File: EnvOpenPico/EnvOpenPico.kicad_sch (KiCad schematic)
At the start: 58 parts, among them J2 TSA343G00-250J2, J3 2.54mm header 01x20, J4 2.54mm header 01x20, J5 Conn_01x03_Male, Q1 SI2301B, U1 SOT-23-5 5.5V 3.3V 500mA, U3 RP2040, Y1 3225_4P

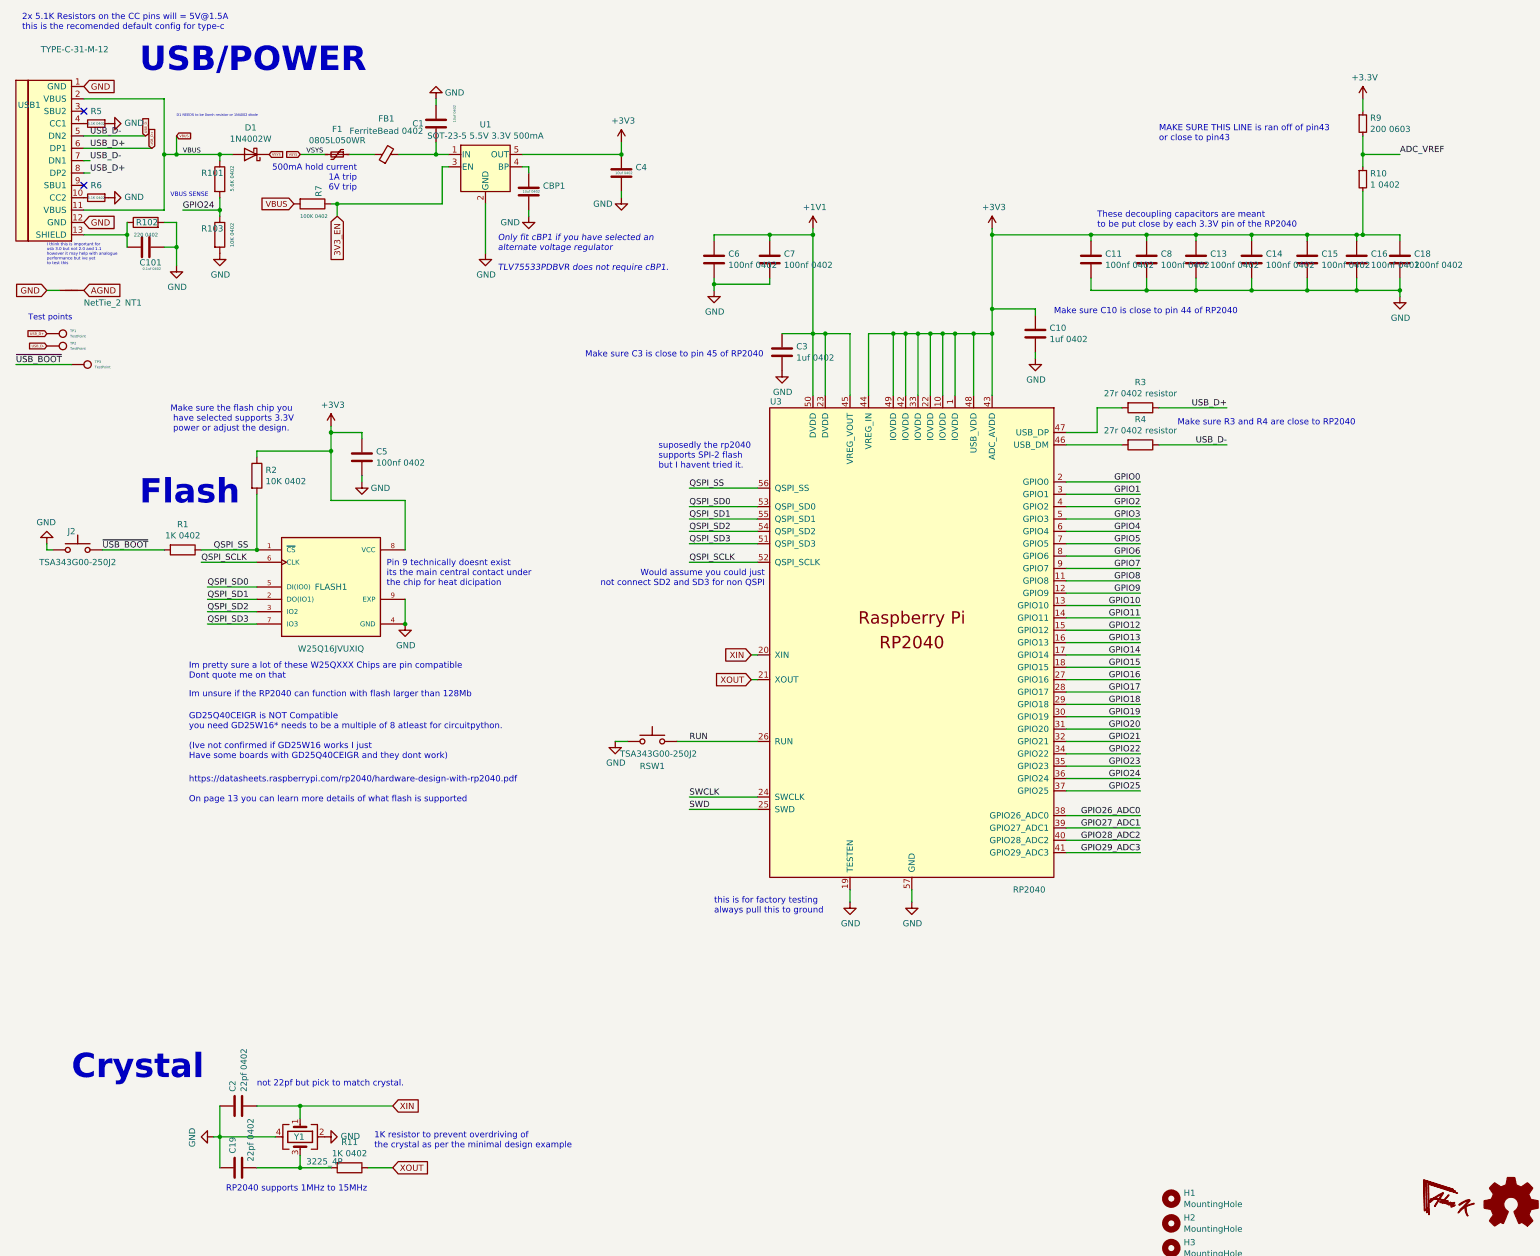
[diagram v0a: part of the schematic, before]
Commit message: replaced flash symbol with built in one, some clearance fixes
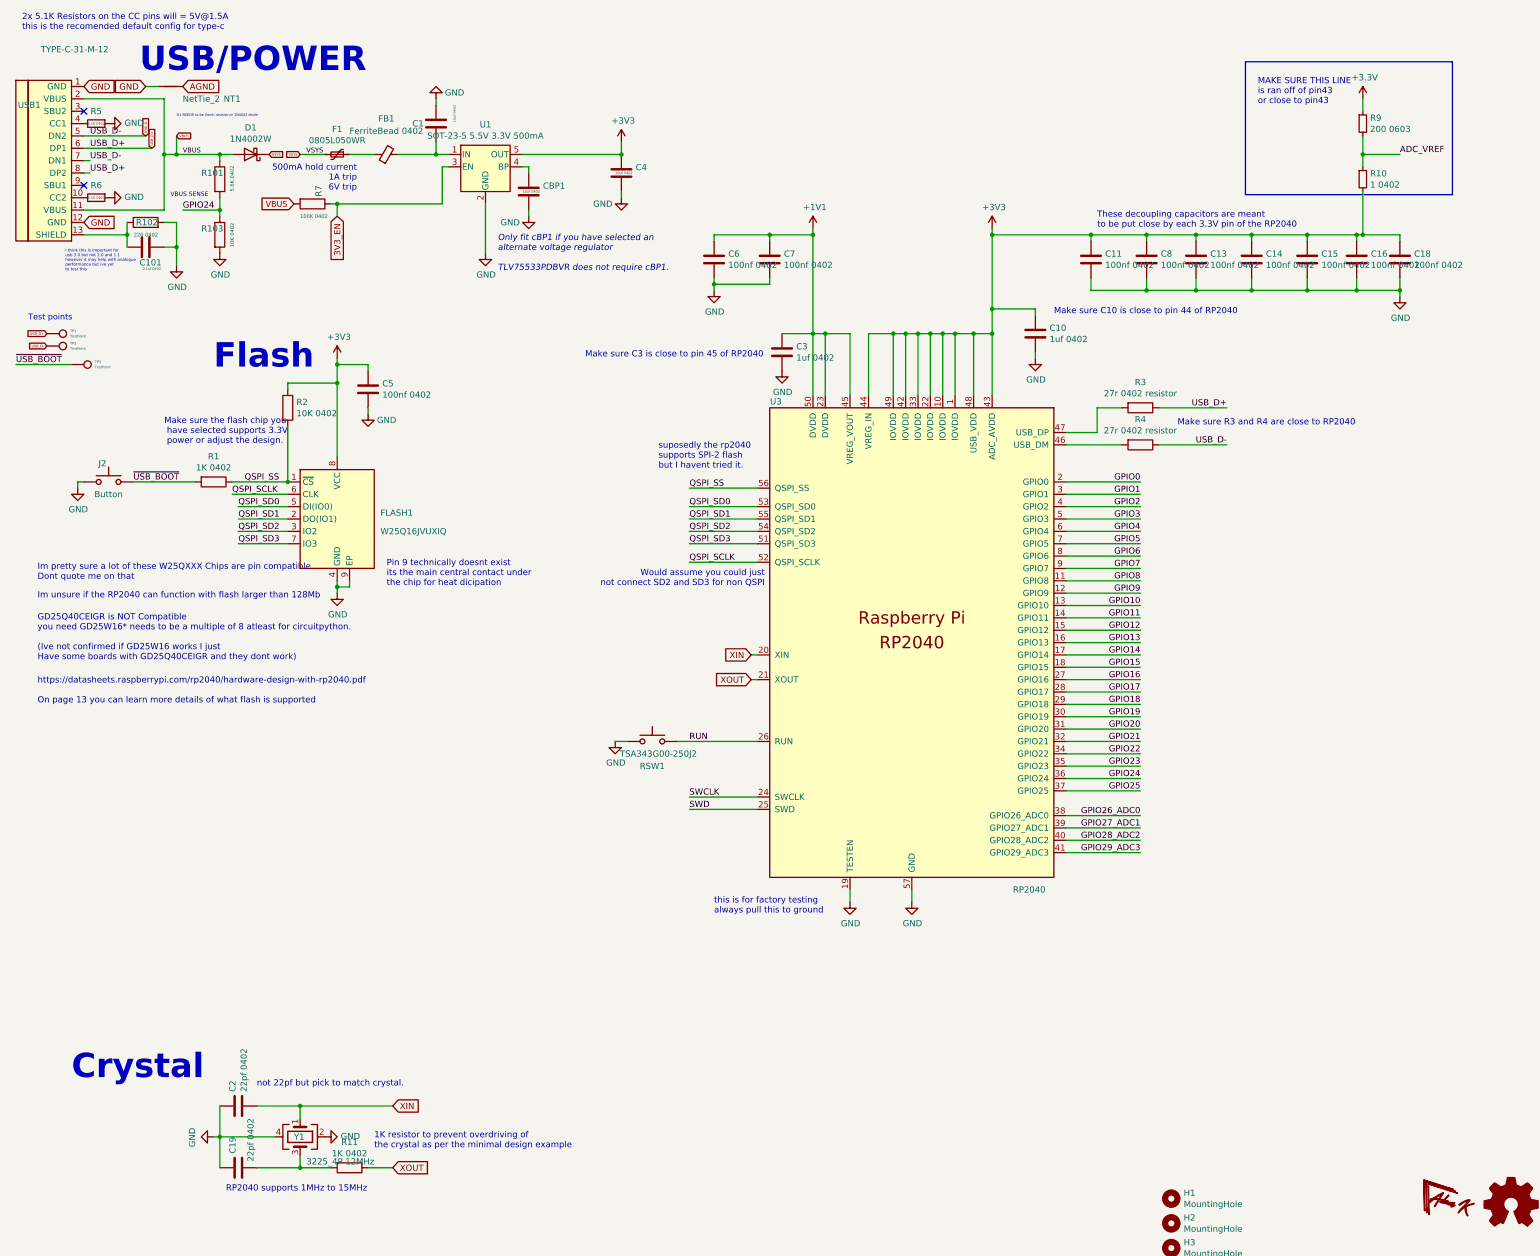
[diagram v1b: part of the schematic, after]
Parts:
- removed FLASH1: W25Q16JVUXIQ, Package_SON:SON-8-1EP_3x2mm_P0.5mm_EP1.4x1.6mm, symbol W25Q256JVEIQ_TR:W25Q256JVEIQ_TR
- added FLASH1: W25Q16JVUXIQ, Package_SON:SON-8-1EP_3x2mm_P0.5mm_EP1.4x1.6mm, symbol Memory_Flash:W25Q32JVZP
- J2: value TSA343G00-250J2 -> Button
- Y1: value 3225_4P -> 3225_4P 12MHz
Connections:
- net +3V3: now also FLASH1.8 (VCC)
- net GND: now also FLASH1.4 (GND), FLASH1.9 (EP)
- net QSPI_SCLK: now also FLASH1.6 (CLK)
- net QSPI_SD0: now also FLASH1.5 (DI(IO0))
- net QSPI_SD1: now also FLASH1.2 (DO(IO1))
- net QSPI_SD2: now also FLASH1.3 (IO2)
- net QSPI_SD3: now also FLASH1.7 (IO3)
- net QSPI_SS: now also FLASH1.1 (~{CS})
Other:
- title: Raspberry Pi Pico Clone -> EnvOpenPico
- moved on the sheet: NT1

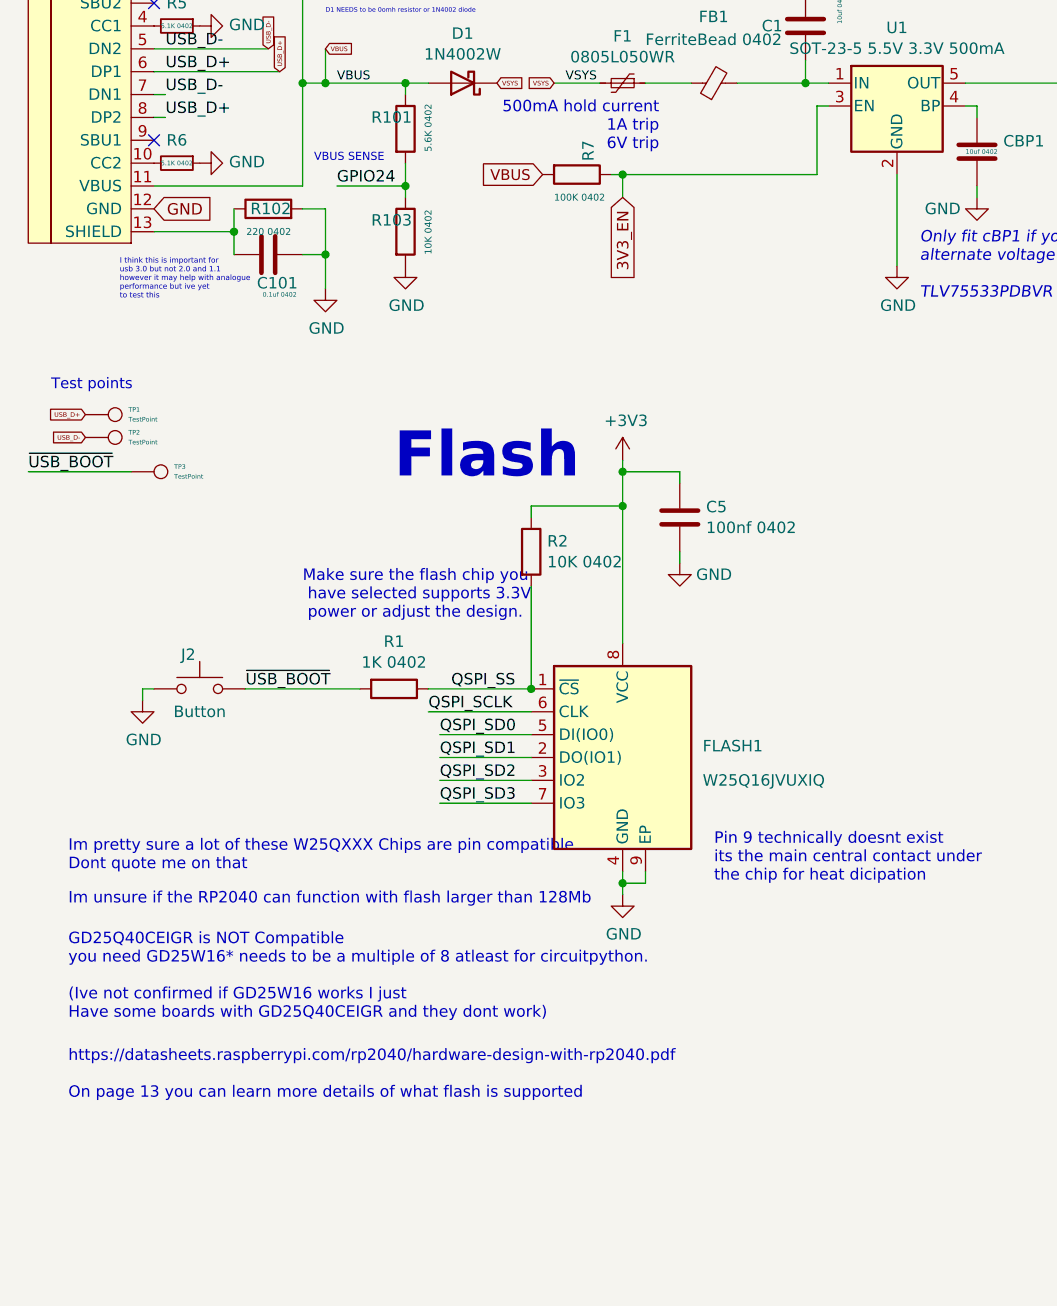
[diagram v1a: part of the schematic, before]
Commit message: fixed major potential oversight on 3V3_EN being tied to VBUS rather than VSYS.
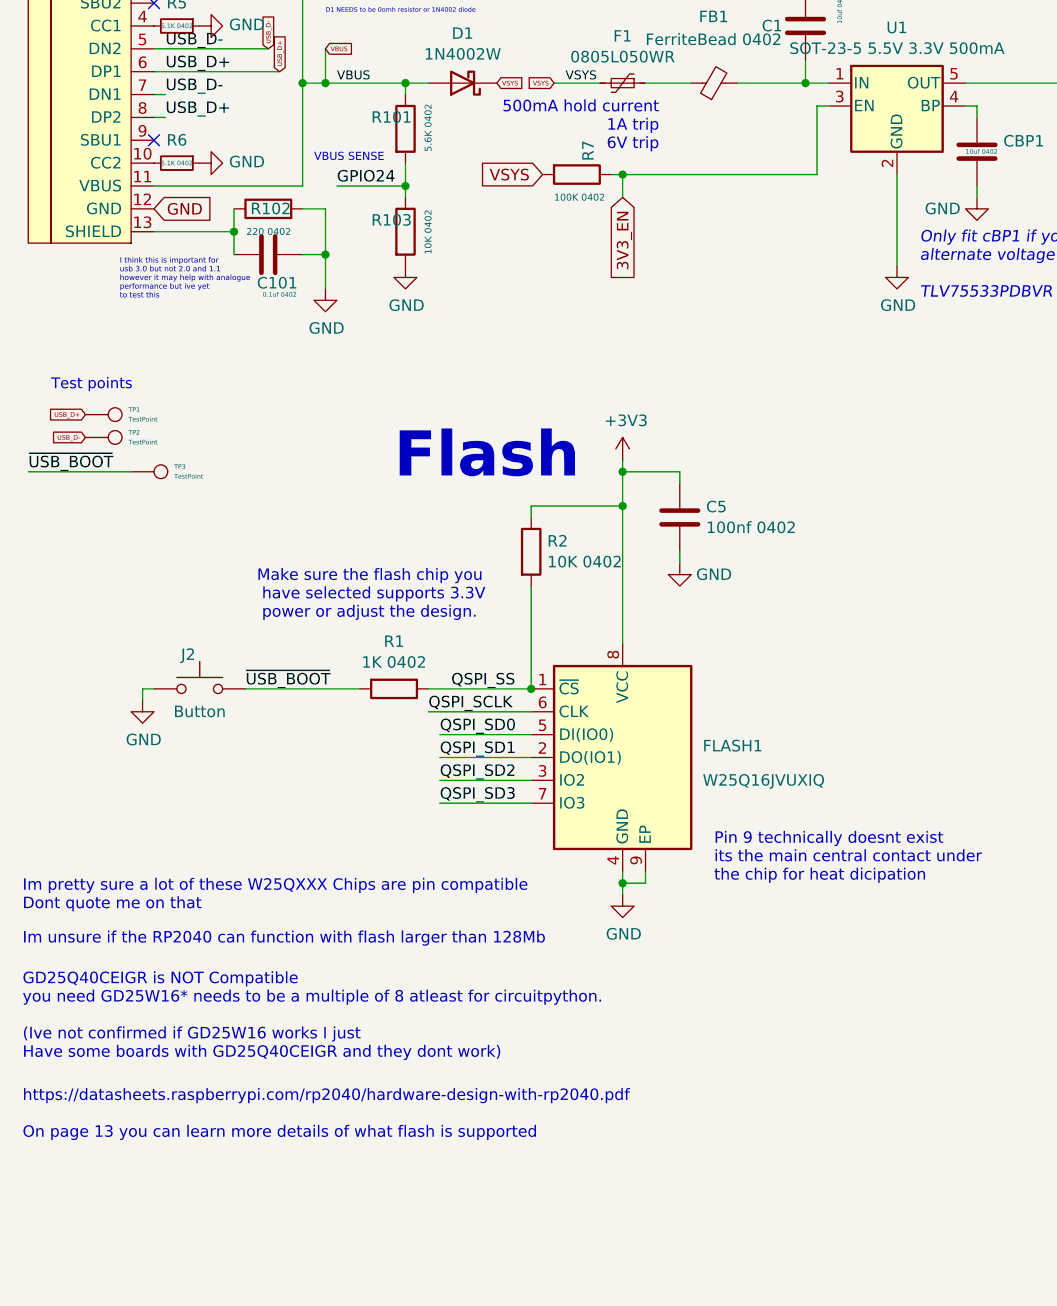
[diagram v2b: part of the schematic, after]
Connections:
- net VBUS: no longer R7.2
- net VSYS: now also R7.2
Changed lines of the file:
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@@
   )
   (text "GD25Q40CEIGR is NOT Compatible\nyou need GD25W16* needs to be a multiple of 8 atleast for circuitpython.\n\n(Ive not confirmed if GD25W16 works I just \nHave some boards with GD25Q40CEIGR and they dont work)"
-    (at 18.415 148.59 0)
+    (at 13.335 153.035 0)
     (effects (font (size 1.27 1.27)) (justify left bottom))
   )
@@
   )
   (text "https://datasheets.raspberrypi.com/rp2040/hardware-design-with-rp2040.pdf\n\nOn page 13 you can learn more details of what flash is supported\n"
-    (at 18.415 157.48 0)
+    (at 13.335 161.925 0)
     (effects (font (size 1.27 1.27)) (justify left bottom))
   )
@@
   )
   (text "Im unsure if the RP2040 can function with flash larger than 128Mb"
-    (at 18.415 135.89 0)
+    (at 13.335 140.335 0)
     (effects (font (size 1.27 1.27)) (justify left bottom))
   )
@@
   )
   (text "Im pretty sure a lot of these W25QXXX Chips are pin compatible\nDont quote me on that"
-    (at 18.415 132.08 0)
+    (at 13.335 136.525 0)
     (effects (font (size 1.27 1.27)) (justify left bottom))
   )
@@
   )
   (text "Make sure the flash chip you\n have selected supports 3.3V\n power or adjust the design."
-    (at 44.45 104.14 0)
+    (at 39.37 104.14 0)
     (effects (font (size 1.27 1.27)) (justify left bottom))
   )
@@
     (effects (font (size 1.27 1.27)) (justify right))
     (property "Intersheetrefs" "${INTERSHEET_REFS}" (at 160.0595 147.32 0)
+      (effects (font (size 1.27 1.27)) (justify right) hide)
+    )
+  )
+  (global_label "VSYS" (shape input) (at 71.12 54.61 180) (fields_autoplaced)
+    (effects (font (size 1.27 1.27)) (justify right))
+    (property "Intersheetrefs" "${INTERSHEET_REFS}" (at 64.2722 54.61 0)
       (effects (font (size 1.27 1.27)) (justify right) hide)
     )
@@
     )
   )
-  (global_label "VBUS" (shape input) (at 71.12 54.61 180) (fields_autoplaced)
-    (effects (font (size 1.1938 1.1938)) (justify right))
-    (property "Intersheetrefs" "${INTERSHEET_REFS}" (at 64.636 54.61 0)
-      (effects (font (size 1.27 1.27)) (justify right) hide)
-    )
-  )

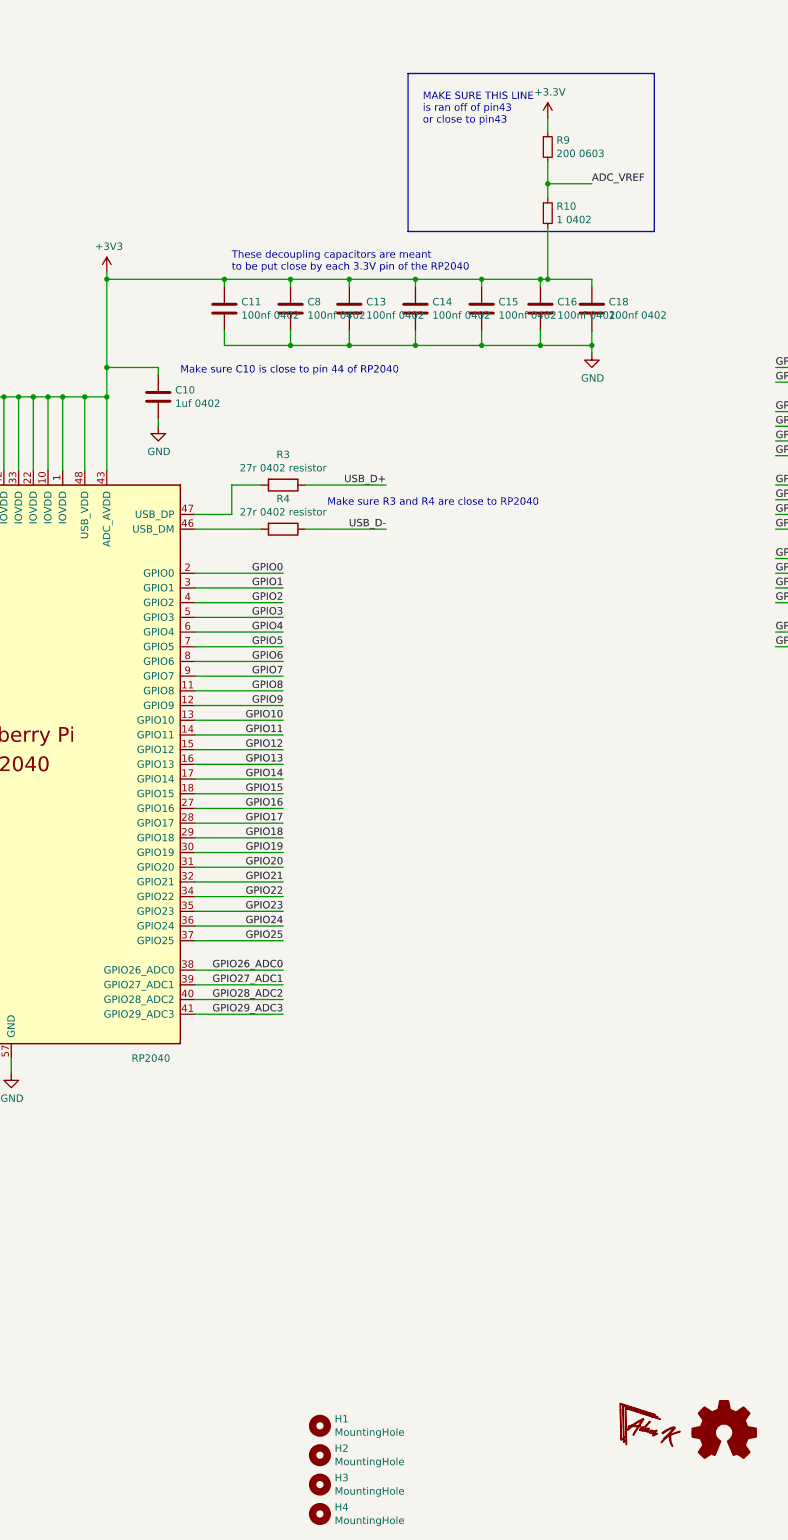
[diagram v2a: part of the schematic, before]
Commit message: fixed ADC_AVDD being tied to 3V3 incorrectly, various tweaks and adjustments to part positions to ensure everything fits properly
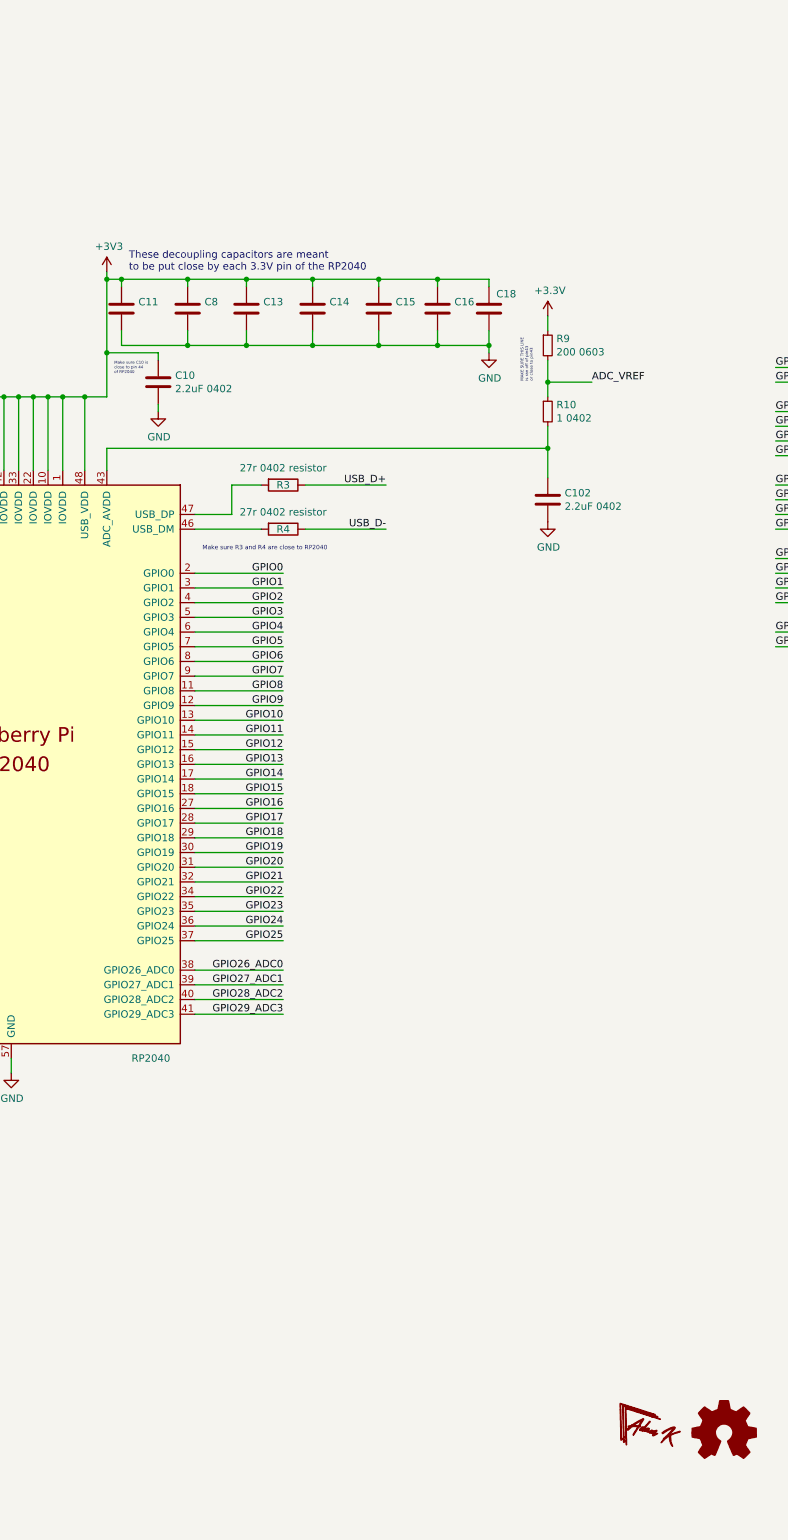
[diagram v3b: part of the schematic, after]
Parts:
- removed H1, H2, H3, H4: MountingHole, MountingHole:MountingHole_2.1mm, symbol Mechanical:MountingHole
- added C102: 2.2uF 0402, Capacitor_SMD:C_0402_1005Metric, symbol Device:C
- C10: value 1uf 0402 -> 2.2uF 0402
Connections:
- net +3V3: no longer R10.2, U3.43 (ADC_AVDD)
- net GND: now also C102.2
- new net: C102.1, R10.2, U3.43 (ADC_AVDD)
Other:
- moved on the sheet: C10, C11, C13, C14, C15, C16, C18, C8, R10, R9
